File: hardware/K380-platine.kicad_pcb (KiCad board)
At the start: 2 copper layers, 98 x 36 mm, 41 parts, among them J1 JST-PH 2, J2 Conn_01x23, J3 MicroMod-M.2E, J4 USB_C_Receptacle_USB2.0, J5 Conn_ARM_JTAG_SWD_10, Q1 PMost Enc FET -20V, Q2 Q_NMOS_DGS, SW1 EG1215AA, SW2 SW_Push, SW3 SW_Push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

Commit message: hardware: schematic: Moved MCU to separate page
With this separation of content, it will make the future change of
directly placing the nRF52840 module onto the board much easier, as all
parts that replace the micromod module will be part of this new sheet.

Signed-off-by: Sophie Friedrich <dev@flowerpot.me>
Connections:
- D3 pad 1: +3V3 -> Net-(D3-DOUT)
- D3 pad 2: Net-(D3-Pad2) -> GND
- D3 pad 3: GND -> DLED
- D3 pad 4: DLED -> +3V3
- D4 pad 1: +3V3 -> Net-(D4-DOUT)
- D4 pad 2: Net-(D4-Pad2) -> GND
- D4 pad 3: GND -> Net-(D3-DOUT)
- D4 pad 4: Net-(D3-Pad2) -> +3V3
- D5 pad 1: +3V3 -> Net-(D5-DOUT)
- D5 pad 2: Net-(D5-Pad2) -> GND
- D5 pad 3: GND -> Net-(D4-DOUT)
- D5 pad 4: Net-(D4-Pad2) -> +3V3
- D6 pad 1: +3V3 -> unconnected-(D6-DOUT-Pad1)
- D6 pad 2: unconnected-(D6-Pad2) -> GND
- D6 pad 3: GND -> Net-(D5-DOUT)
- D6 pad 4: Net-(D5-Pad2) -> +3V3
- J3 pad 15: unconnected-(J3-Pad15) -> /CPU/P1.09
- J3 pad 17: unconnected-(J3-Pad17) -> /CPU/P1.03
- J3 pad 19: unconnected-(J3-Pad19) -> /CPU/P1.10
- J3 pad 47: unconnected-(J3-Pad47) -> /CPU/P0.16
- J3 pad 50: unconnected-(J3-Pad50) -> /CPU/P0.25
- J3 pad 51: unconnected-(J3-Pad51) -> /CPU/P1.01
- J3 pad 53: unconnected-(J3-Pad53) -> /CPU/P0.24
- J3 pad 55: unconnected-(J3-Pad55) -> /CPU/P0.20
- J3 pad 57: unconnected-(J3-Pad57) -> /CPU/P0.28(AIN4)
- VUSB1 pad 1: VUSB -> VBUS
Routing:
- net (no net): track 0.00 -> 62.7 mm
- net Net-(D5-Pad2): track 29.2 -> 0.00 mm, vias 1 -> 0
- net Net-(D3-Pad2): track 17.4 -> 0.00 mm
- net Net-(D4-Pad2): track 16.1 -> 0.00 mm
- net GND: track 95.2 -> 93.1 mm, vias 25 -> 24
- net Net-(D5-DOUT): track 0.00 -> 2.15 mm, vias 0 -> 1
- net +3V3: vias 8 -> 9

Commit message: hardware: first nRF52840 raw tries
The current schematic should (in theory) be a complete setup for the
nRF52840 chip with power and everything.

In the footprint first routing attempts have been made, but this has
been without real success for now, especially as the nRF52840 is a hell
of a chip to implement. Ignoring the whole "need to do own RF" here,
it's almost impossible to get the inner pins out from under the chip
without paying extra for either via-in-pads or precision milling.

I'll leave this commit here for an exemplary routing of (some) inner
GPIO pins off the nRF52840 while presumably being in spec of JLCPCBs
capabilities. I want this project to come to an end, so I'll step away
from implementing my own nRF52840, and buy a carrier module with it
instead.

And yeah - RF stuff is magic and mostly consists of dark incantations.
The major advantage of buying a carrier board that already does the RF
for me, is that I have fewer requirements on the PCB manufacturer and
people can just manufacture it with their favorite producer.

Signed-off-by: Sophie Friedrich <dev@flowerpot.me>
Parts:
- removed J3: MicroMod-M.2E, SparkFun MicroMod:M.2-CONNECTOR-E
- added AE1: Antenna_Shield, RF_Antenna:Texas_SWRA117D_2.4GHz_Right, F.Cu at (82.7, 70.1)
- added C10: 12pF, Capacitor_SMD:C_0603_1608Metric_Pad1.08x0.95mm_HandSolder, F.Cu at (47.7, 59.0)
- added C11: 4.7uF, Capacitor_SMD:C_0603_1608Metric_Pad1.08x0.95mm_HandSolder, F.Cu at (47.7, 61.6)
- added C12: 100nF, Capacitor_SMD:C_0603_1608Metric_Pad1.08x0.95mm_HandSolder, F.Cu at (47.7, 64.1)
- added C13: 1.0pF, Capacitor_SMD:C_0603_1608Metric_Pad1.08x0.95mm_HandSolder, F.Cu at (64.3, 71.0)
- added C14: 1uF, Capacitor_SMD:C_0603_1608Metric_Pad1.08x0.95mm_HandSolder, F.Cu at (47.7, 69.1)
- added C15: 47n, Capacitor_SMD:C_0603_1608Metric_Pad1.08x0.95mm_HandSolder, F.Cu at (52.0, 51.5)
- added C16: 1uF, Capacitor_SMD:C_0603_1608Metric_Pad1.08x0.95mm_HandSolder, F.Cu at (52.0, 54.0)
- added C17: 4.7uF, Capacitor_SMD:C_0603_1608Metric_Pad1.08x0.95mm_HandSolder, F.Cu at (52.0, 56.5)
- added C19: 100pF, Capacitor_SMD:C_0603_1608Metric_Pad1.08x0.95mm_HandSolder, F.Cu at (52.0, 61.6)
- added C20: 100nF, Capacitor_SMD:C_0603_1608Metric_Pad1.08x0.95mm_HandSolder, F.Cu at (52.0, 64.1)
- added C21: 1.2pF, Capacitor_SMD:C_0603_1608Metric_Pad1.08x0.95mm_HandSolder, F.Cu at (68.3, 71.0)
- added C25: 100nF, Capacitor_SMD:C_0603_1608Metric_Pad1.08x0.95mm_HandSolder, F.Cu at (52.0, 69.1)
- added C26: 100nF, Capacitor_SMD:C_0603_1608Metric_Pad1.08x0.95mm_HandSolder, F.Cu at (56.4, 51.5)
- added C7: 12pF, Capacitor_SMD:C_0603_1608Metric_Pad1.08x0.95mm_HandSolder, F.Cu at (47.7, 51.5)
- added C8: 12pF, Capacitor_SMD:C_0603_1608Metric_Pad1.08x0.95mm_HandSolder, F.Cu at (47.7, 54.0)
- added C9: 12pF, Capacitor_SMD:C_0603_1608Metric_Pad1.08x0.95mm_HandSolder, F.Cu at (47.7, 56.5)
- added L1: 15nH, Inductor_SMD:L_0603_1608Metric, F.Cu at (69.2, 60.0)
- added L2: 10uH, Inductor_SMD:L_0603_1608Metric, F.Cu at (69.2, 62.5)
- added L3: 4.7nH, Inductor_SMD:L_0603_1608Metric, F.Cu at (66.4, 70.1)
- added L4: 2.2nH, Inductor_SMD:L_0603_1608Metric, F.Cu at (62.4, 70.1)
- added R10: 10k, Capacitor_SMD:C_0603_1608Metric_Pad1.08x0.95mm_HandSolder, F.Cu at (56.4, 54.0)
- added R11: 10k, Capacitor_SMD:C_0603_1608Metric_Pad1.08x0.95mm_HandSolder, F.Cu at (56.4, 56.5)
- added R12: 270, Capacitor_SMD:C_0603_1608Metric_Pad1.08x0.95mm_HandSolder, F.Cu at (56.4, 59.0)
- added R13: 270, Capacitor_SMD:C_0603_1608Metric_Pad1.08x0.95mm_HandSolder, F.Cu at (56.4, 61.6)
- added U3: nRF52840, Package_DFN_QFN:Nordic_AQFN-73-1EP_7x7mm_P0.5mm, F.Cu at (91.5, 79.4)
- added Y1: 32.768kHz, Capacitor_SMD:C_0603_1608Metric_Pad1.08x0.95mm_HandSolder, F.Cu at (56.4, 64.1)
- added Y2: 32MHz, Crystal:Crystal_SMD_2520-4Pin_2.5x2.0mm, F.Cu at (64.4, 45.2)
- U2: footprint Package_TO_SOT_SMD:SOT-23-5_HandSoldering -> Package_TO_SOT_SMD:SOT-23-5
- moved R8 27.7 mm to (64.1, 79.5)
- moved R9 27.7 mm to (64.1, 77.8)
- moved J5 21.5 mm to (95.0, 50.3), turned to 0 degrees
- moved C5 1.43 mm to (111.9, 68.8)
- moved D5 0.42 mm to (150.4, 67.9), turned to -90 degrees
- moved D3 0.30 mm to (114.8, 68.2), turned to -90 degrees
- turned D4 to -90 degrees
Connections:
- net +3V3 renamed +3.3V
- J5 pad 2: SWDIO -> Net-(J5-SWDIO/TMS)
- J5 pad 4: SWDCLK -> Net-(J5-SWDCLK/TCK)
- J5 pad 6: /SWO -> /CPU/SWO
- VBAT1 pad 1: VBAT -> +BATT
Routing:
- net (no net): track 62.7 -> 0.00 mm
- net GND: track 93.1 -> 51.9 mm, vias 24 -> 22
- net RESET: track 54.7 -> 21.7 mm, vias 2 -> 1
- net VBUS: track 114.8 -> 83.4 mm, vias 2 -> 1
- net Net-(D5-DOUT): track 2.15 -> 29.2 mm, vias 1 -> 3
- net SWDCLK: track 24.7 -> 0.00 mm
- net D+: track 69.0 -> 44.9 mm, vias 2 -> 0
- net SWDIO: track 22.8 -> 0.00 mm
- net D-: track 69.5 -> 47.0 mm, vias 2 -> 0
- net Net-(D4-DOUT): track 0.00 -> 17.5 mm
- net Net-(D3-DOUT): track 0.00 -> 17.5 mm
- net +BATT: track 141.6 -> 127.8 mm, vias 4 -> 3
- net ROW1: track 51.7 -> 42.4 mm, vias 2 -> 1
- net ROW2: track 52.1 -> 43.7 mm, vias 2 -> 1
- net ROW3: track 52.7 -> 45.0 mm, vias 2 -> 1
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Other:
- copper layers 2 -> 4

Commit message: Revert "hardware: first nRF52840 raw tries"
Wanna start from a clean slate. See referenced commit on why I'm doing
this.

This reverts commit 5420c1d1e1bdfd9146d776c48bdd16e2d166426d.
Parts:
- removed AE1: Antenna_Shield, RF_Antenna:Texas_SWRA117D_2.4GHz_Right
- removed C10, C7, C8, C9: 12pF, Capacitor_SMD:C_0603_1608Metric_Pad1.08x0.95mm_HandSolder
- removed C11, C17: 4.7uF, Capacitor_SMD:C_0603_1608Metric_Pad1.08x0.95mm_HandSolder
- removed C12, C20, C25, C26: 100nF, Capacitor_SMD:C_0603_1608Metric_Pad1.08x0.95mm_HandSolder
- removed C13: 1.0pF, Capacitor_SMD:C_0603_1608Metric_Pad1.08x0.95mm_HandSolder
- removed C14, C16: 1uF, Capacitor_SMD:C_0603_1608Metric_Pad1.08x0.95mm_HandSolder
- removed C15: 47n, Capacitor_SMD:C_0603_1608Metric_Pad1.08x0.95mm_HandSolder
- removed C19: 100pF, Capacitor_SMD:C_0603_1608Metric_Pad1.08x0.95mm_HandSolder
- removed C21: 1.2pF, Capacitor_SMD:C_0603_1608Metric_Pad1.08x0.95mm_HandSolder
- removed L1: 15nH, Inductor_SMD:L_0603_1608Metric
- removed L2: 10uH, Inductor_SMD:L_0603_1608Metric
- removed L3: 4.7nH, Inductor_SMD:L_0603_1608Metric
- removed L4: 2.2nH, Inductor_SMD:L_0603_1608Metric
- removed R10, R11: 10k, Capacitor_SMD:C_0603_1608Metric_Pad1.08x0.95mm_HandSolder
- removed R12, R13: 270, Capacitor_SMD:C_0603_1608Metric_Pad1.08x0.95mm_HandSolder
- removed U3: nRF52840, Package_DFN_QFN:Nordic_AQFN-73-1EP_7x7mm_P0.5mm
- removed Y1: 32.768kHz, Capacitor_SMD:C_0603_1608Metric_Pad1.08x0.95mm_HandSolder
- removed Y2: 32MHz, Crystal:Crystal_SMD_2520-4Pin_2.5x2.0mm
- added J3: MicroMod-M.2E, SparkFun MicroMod:M.2-CONNECTOR-E, F.Cu at (102.4, 81.7)
- U2: footprint Package_TO_SOT_SMD:SOT-23-5 -> Package_TO_SOT_SMD:SOT-23-5_HandSoldering
- moved R8 27.7 mm to (91.8, 77.2)
- moved R9 27.7 mm to (91.8, 75.5)
- moved J5 21.5 mm to (85.2, 69.5), turned to -90 degrees
- moved C5 1.43 mm to (112.1, 70.2)
- moved D5 0.42 mm to (150.0, 68.0), turned to 0 degrees
- moved D3 0.30 mm to (114.6, 68.0), turned to 0 degrees
- turned D4 to 0 degrees
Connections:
- net +3.3V renamed +3V3
- J5 pad 2: Net-(J5-SWDIO/TMS) -> SWDIO
- J5 pad 4: Net-(J5-SWDCLK/TCK) -> SWDCLK
- J5 pad 6: /CPU/SWO -> /SWO
- VBAT1 pad 1: +BATT -> VBAT
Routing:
- net (no net): track 0.00 -> 62.7 mm
- net GND: track 51.9 -> 93.1 mm, vias 22 -> 24
- net RESET: track 21.7 -> 54.7 mm, vias 1 -> 2
- net VBUS: track 83.4 -> 114.8 mm, vias 1 -> 2
- net Net-(D5-DOUT): track 29.2 -> 2.15 mm, vias 3 -> 1
- net SWDCLK: track 0.00 -> 24.7 mm
- net D+: track 44.9 -> 69.0 mm, vias 0 -> 2
- net SWDIO: track 0.00 -> 22.8 mm
- net D-: track 47.0 -> 69.5 mm, vias 0 -> 2
- net Net-(D4-DOUT): track 17.5 -> 0.00 mm
- net Net-(D3-DOUT): track 17.5 -> 0.00 mm
- net +BATT: track 127.8 -> 141.6 mm, vias 3 -> 4
- net ROW1: track 42.4 -> 51.7 mm, vias 1 -> 2
- net ROW2: track 43.7 -> 52.1 mm, vias 1 -> 2
- net ROW3: track 45.0 -> 52.7 mm, vias 1 -> 2
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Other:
- copper layers 4 -> 2

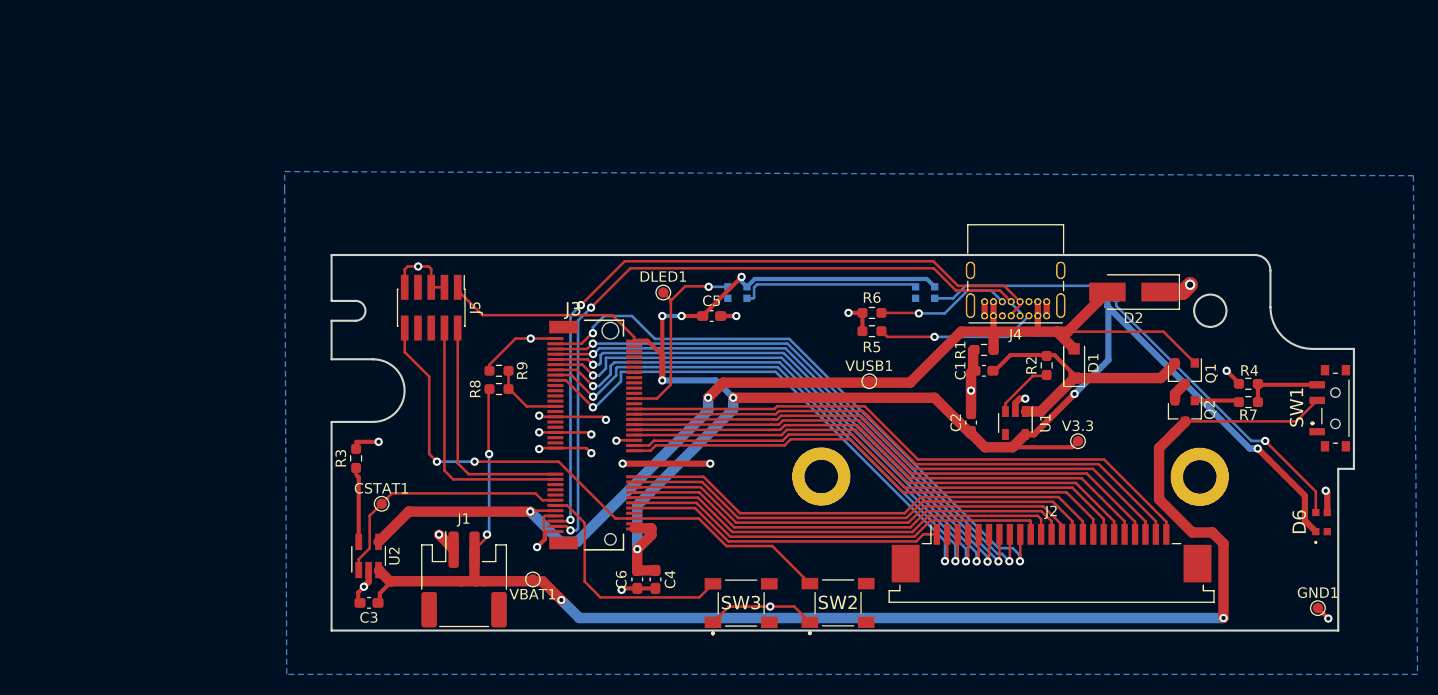
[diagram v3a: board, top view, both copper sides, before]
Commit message: hardware: completed rev 0.2α (pre-verify)
This is a bigger change from the iteration. The MicroMod has been
replaced with an HolyIoT nRF52840, which can be directly soldered onto
the board. This guarantees minimal space usage, while reducing the
complexity to implement an MCU on our own.

Additionally this iteration moves away from reserving a gpio port per
keyboard matrix trace, and instead makes use of an GPIO shift register
(74AHC595A). They are quite popular and also have support in ZMK since a
few weeks ago.

This commit adheres to the design rules for a 2 layer PCB and passes all
DRC checks.

Signed-off-by: Sophie Friedrich <dev@flowerpot.me>
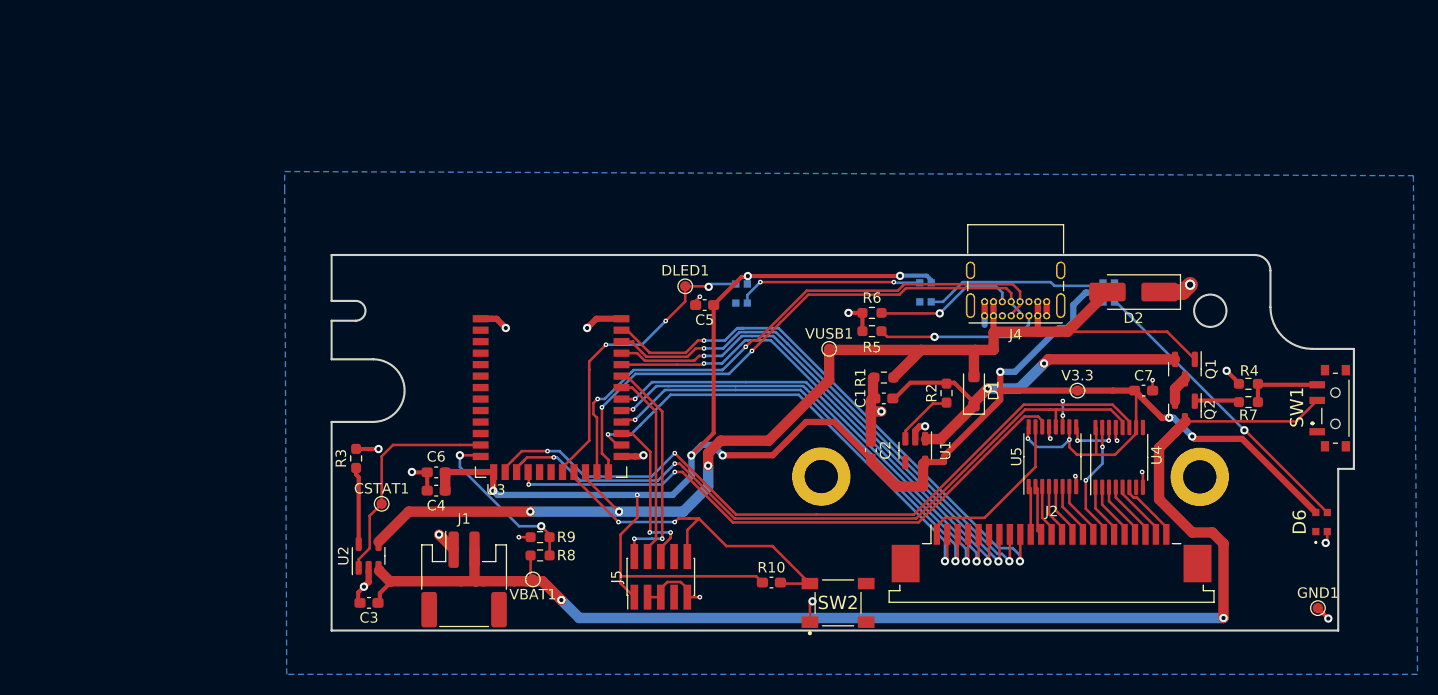
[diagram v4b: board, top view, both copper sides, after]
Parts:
- removed J3: MicroMod-M.2E, SparkFun MicroMod:M.2-CONNECTOR-E
- removed SW3: SW_Push, LibraryLoader:MJTP1140AAUTR - Fixed
- added C7: 100uF, Capacitor_SMD:C_0603_1608Metric_Pad1.08x0.95mm_HandSolder, F.Cu at (153.5, 77.4)
- added R10: 10k, Capacitor_SMD:C_0603_1608Metric_Pad1.08x0.95mm_HandSolder, F.Cu at (117.9, 95.8)
- added U3: nRF52840_holyiot_18010, PCM_marbastlib-various:nRF52840_holyiot_18010_HS_simple, F.Cu at (96.7, 76.2)
- added U4: 74AHC595, Package_SO:TSSOP-16_4.4x5mm_P0.65mm, F.Cu at (151.2, 83.8)
- added U5: 74AHC595, Package_SO:TSSOP-16_4.4x5mm_P0.65mm, F.Cu at (144.8, 83.7)
- H1, H2: renamed from REF**; value MountingHole_3.2mm_M3_DIN965_Pad -> MountingHole
- U2: footprint Package_TO_SOT_SMD:SOT-23-5_HandSoldering -> Package_TO_SOT_SMD:SOT-23-5
- moved J5 33.9 mm to (107.3, 95.2), turned to 90 degrees
- moved C4 22.7 mm to (85.7, 87.0), turned to 180 degrees
- moved C6 21.8 mm to (85.7, 85.2), turned to 180 degrees
- moved R8 16.4 mm to (95.7, 93.2)
- moved R9 16.4 mm to (95.7, 91.5)
- moved C1 9.96 mm to (128.6, 78.2)
- moved D1 9.96 mm to (137.3, 77.5)
- moved R1 9.96 mm to (128.7, 76.2)
- moved R2 9.96 mm to (134.7, 77.6)
- moved U1 9.96 mm to (131.7, 83.2)
- moved C2 9.96 mm to (127.4, 83.1)
- moved VUSB1 4.94 mm to (123.4, 73.4)
- moved V3.3 4.85 mm to (147.2, 77.4)
- moved DLED1 2.18 mm to (109.6, 67.4)
- moved C5 1.25 mm to (111.5, 69.2), turned to 180 degrees
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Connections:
- net +3V3 renamed +3.3V
- net CSTAT renamed /CSTAT
- net D+ renamed /D+
- net D- renamed /D-
- net DLED renamed /DLED
- net RESET renamed /RESET
- net VDIV renamed /VDIV
- J2 pad 1: COL1 -> /COL1
- J2 pad 10: COL2 -> /COL2
- J2 pad 11: COL3 -> /COL3
- J2 pad 12: COL4 -> /COL4
- J2 pad 13: COL5 -> /COL5
- J2 pad 14: COL6 -> /COL6
- J2 pad 15: COL7 -> /COL7
- J2 pad 16: COL8 -> /COL8
- J2 pad 17: COL9 -> /COL9
- J2 pad 18: COL10 -> /COL10
- J2 pad 19: COL11 -> /COL11
- J2 pad 2: ROW1 -> /ROW1
- J2 pad 20: COL12 -> /COL12
- J2 pad 21: COL13 -> /COL13
- J2 pad 22: COL14 -> /COL14
- J2 pad 23: COL15 -> /COL15
- J2 pad 3: ROW2 -> /ROW2
- J2 pad 4: ROW3 -> /ROW3
- J2 pad 5: ROW4 -> /ROW4
- J2 pad 6: ROW5 -> /ROW5
- J2 pad 7: ROW6 -> /ROW6
- J2 pad 8: ROW7 -> /ROW7
- J2 pad 9: ROW8 -> /ROW8
- J5 pad 2: SWDIO -> /SWDIO
- J5 pad 4: SWDCLK -> /SWDCLK
- VBAT1 pad 1: VBAT -> +BATT
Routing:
- net /LS_SCK: track 0.00 -> 73.7 mm, vias 0 -> 4
- net /LS_EN: track 0.00 -> 70.4 mm, vias 0 -> 2
- net (no net): track 62.7 -> 0.00 mm
- net ROW8: track 58.6 -> 0.00 mm, vias 2 -> 0
- net /LS_MOSI: track 0.00 -> 57.9 mm, vias 0 -> 2
- net COL15: track 56.9 -> 0.00 mm
- net COL14: track 56.2 -> 0.00 mm
- net ROW7: track 55.0 -> 0.00 mm, vias 2 -> 0
- net COL13: track 54.6 -> 0.00 mm
- net ROW6: track 53.8 -> 0.00 mm, vias 2 -> 0
- net ROW5: track 53.8 -> 0.00 mm, vias 2 -> 0
- net COL12: track 53.4 -> 0.00 mm
- net ROW4: track 53.4 -> 0.00 mm, vias 2 -> 0
- net /ROW8: track 0.00 -> 52.9 mm, vias 0 -> 2
- net ROW3: track 52.7 -> 0.00 mm, vias 2 -> 0
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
